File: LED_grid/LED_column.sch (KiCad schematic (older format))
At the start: 11 parts

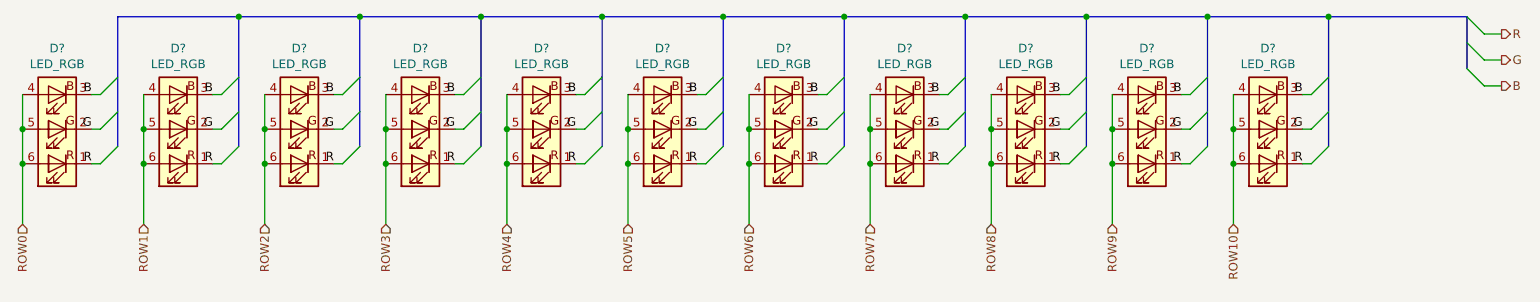
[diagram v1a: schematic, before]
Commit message: Added extra columns to grid along with 5V pin to connectors
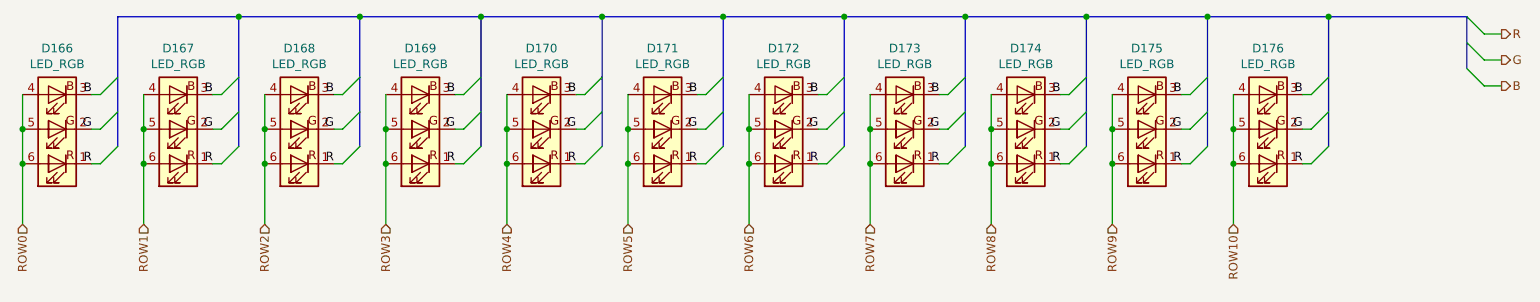
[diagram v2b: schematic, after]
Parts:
- gave numbers to parts that had none: 11
